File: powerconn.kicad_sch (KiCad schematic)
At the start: 13 parts, among them CN1 Conn_01x01, CN2 Conn_01x01, CN3 Conn_01x01, K1 HF32FV-16/5-HLTF(590), Q1 MMBT3904

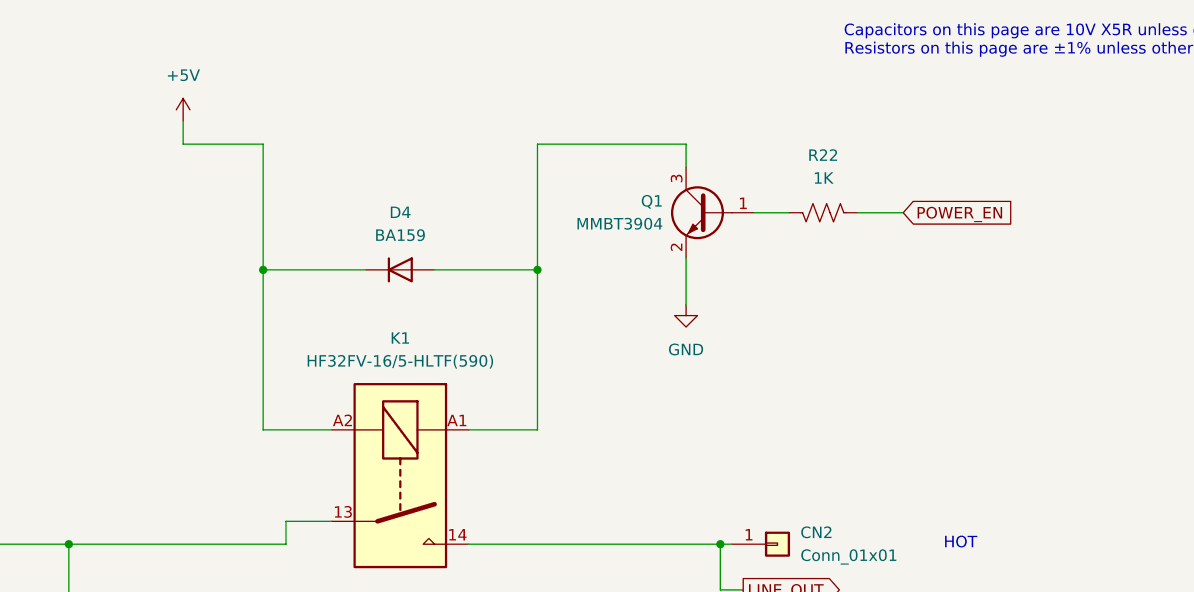
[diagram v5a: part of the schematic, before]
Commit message: All values determined for schematic. From measurements, datasheets, or reading markings.
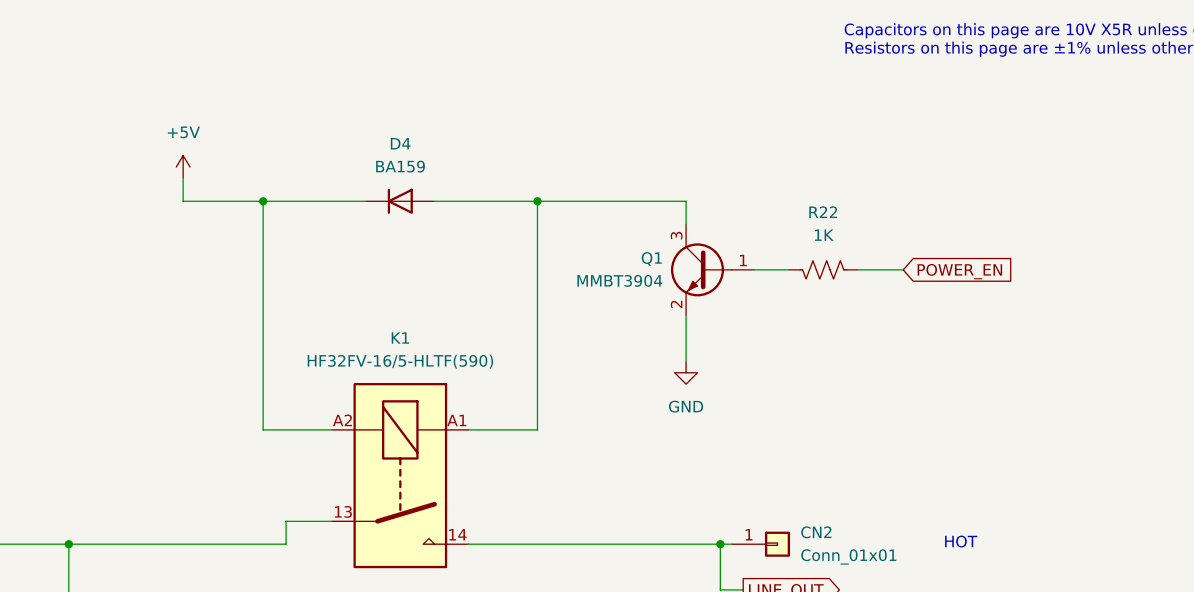
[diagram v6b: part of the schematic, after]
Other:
- moved on the sheet: D4, Q1, R22
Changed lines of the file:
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@@
 	)
 	(junction
-		(at 165.1 52.07)
+		(at 134.62 44.45)
 		(diameter 0)
 		(color 0 0 0 0)
@@
 	)
 	(junction
-		(at 134.62 52.07)
+		(at 165.1 44.45)
 		(diameter 0)
 		(color 0 0 0 0)
@@
 	(wire
 		(pts
-			(xy 153.67 52.07) (xy 165.1 52.07)
+			(xy 153.67 44.45) (xy 165.1 44.45)
 		)
 		(stroke
@@
 	(wire
 		(pts
-			(xy 181.61 38.1) (xy 181.61 40.64)
+			(xy 181.61 44.45) (xy 181.61 46.99)
 		)
 		(stroke
@@
 	(wire
 		(pts
-			(xy 205.74 45.72) (xy 200.66 45.72)
+			(xy 205.74 52.07) (xy 200.66 52.07)
 		)
 		(stroke
@@
 	(wire
 		(pts
-			(xy 181.61 38.1) (xy 165.1 38.1)
-		)
-		(stroke
-			(width 0)
-			(type default)
-		)
-	)
-	(wire
-		(pts
-			(xy 193.04 45.72) (xy 189.23 45.72)
+			(xy 181.61 44.45) (xy 165.1 44.45)
+		)
+		(stroke
+			(width 0)
+			(type default)
+		)
+	)
+	(wire
+		(pts
+			(xy 193.04 52.07) (xy 189.23 52.07)
 		)
 		(stroke
@@
 	(wire
 		(pts
-			(xy 134.62 38.1) (xy 134.62 52.07)
-		)
-		(stroke
-			(width 0)
-			(type default)
-		)
-	)
-	(wire
-		(pts
-			(xy 125.73 35.56) (xy 125.73 38.1)
+			(xy 125.73 41.91) (xy 125.73 44.45)
 		)
 		(stroke
@@
 	(wire
 		(pts
-			(xy 134.62 52.07) (xy 146.05 52.07)
+			(xy 134.62 44.45) (xy 146.05 44.45)
 		)
 		(stroke
@@
 	(wire
 		(pts
-			(xy 165.1 38.1) (xy 165.1 52.07)
-		)
-		(stroke
-			(width 0)
-			(type default)
-		)
-	)
-	(wire
-		(pts
 			(xy 157.48 82.55) (xy 185.42 82.55)
 		)
@@
 	(wire
 		(pts
-			(xy 134.62 52.07) (xy 134.62 69.85)
-		)
-		(stroke
-			(width 0)
-			(type default)
-		)
-	)
-	(wire
-		(pts
-			(xy 165.1 52.07) (xy 165.1 69.85)
-		)
-		(stroke
-			(width 0)
-			(type default)
-		)
-	)
-	(wire
-		(pts
-			(xy 181.61 50.8) (xy 181.61 55.88)
+			(xy 165.1 44.45) (xy 165.1 69.85)
+		)
+		(stroke
+			(width 0)
+			(type default)
+		)
+	)
+	(wire
+		(pts
+			(xy 181.61 57.15) (xy 181.61 62.23)
 		)
 		(stroke
@@
 	(wire
 		(pts
-			(xy 125.73 38.1) (xy 134.62 38.1)
+			(xy 125.73 44.45) (xy 134.62 44.45)
 		)
 		(stroke
@@
 		(pts
 			(xy 137.16 80.01) (xy 142.24 80.01)
+		)
+		(stroke
+			(width 0)
+			(type default)
+		)
+	)
+	(wire
+		(pts
+			(xy 134.62 44.45) (xy 134.62 69.85)
 		)
 		(stroke
@@
 	(global_label "POWER_EN"
 		(shape input)
-		(at 205.74 45.72 0)
+		(at 205.74 52.07 0)
 		(fields_autoplaced yes)
 		(effects
@@
 		)
 		(property "Intersheetrefs" "${INTERSHEET_REFS}"
-			(at 218.6432 45.72 0)
+			(at 218.6432 52.07 0)
 			(effects
 				(font
@@
 	(symbol
 		(lib_id "Diode:BA159")
-		(at 149.86 52.07 0)
+		(at 149.86 44.45 0)
 		(unit 1)
 		(exclude_from_sim no)
@@
 		(fields_autoplaced yes)
 		(property "Reference" "D4"
-			(at 149.86 45.72 0)
+			(at 149.86 38.1 0)
 			(effects
 				(font
@@
 		)
 		(property "Value" "BA159"
-			(at 149.86 48.26 0)
+			(at 149.86 40.64 0)
 			(effects
 				(font
@@
 		)
 		(property "Footprint" "Diode_SMD:D_SOD-123F"
-			(at 149.86 56.515 0)
+			(at 149.86 48.895 0)
 			(effects
 				(font
@@
 		)
 		(property "Datasheet" "https://www.vishay.com/docs/88536/ba157.pdf"
-			(at 149.86 52.07 0)
+			(at 149.86 44.45 0)
 			(effects
 				(font
@@
 		)
 		(property "Description" "1000V 1A Fast recovery Rectifier Diode, DO-41"
-			(at 149.86 52.07 0)
+			(at 149.86 44.45 0)
 			(effects
 				(font
@@
 		)
 		(property "Sim.Device" "D"
-			(at 149.86 52.07 0)
+			(at 149.86 44.45 0)
 			(effects
 				(font
@@
 		)
 		(property "Sim.Pins" "1=K 2=A"
-			(at 149.86 52.07 0)
+			(at 149.86 44.45 0)
 			(effects
 				(font
@@
 	(symbol
 		(lib_id "Device:R_US")
-		(at 196.85 45.72 270)
+		(at 196.85 52.07 270)
 		(mirror x)
 		(unit 1)
@@
 		(fields_autoplaced yes)
 		(property "Reference" "R22"
-			(at 196.85 39.37 90)
+			(at 196.85 45.72 90)
 			(effects
 				(font
@@
 		)
 		(property "Value" "1K"
-			(at 196.85 41.91 90)
+			(at 196.85 48.26 90)
 			(effects
 				(font
@@
 		)
 		(property "Footprint" "Resistor_SMD:R_0402_1005Metric"
-			(at 196.596 44.704 90)
+			(at 196.596 51.054 90)
 			(effects
 				(font
@@
 		)
 		(property "Datasheet" "~"
-			(at 196.85 45.72 0)
+			(at 196.85 52.07 0)
 			(effects
 				(font
@@
 		)
 		(property "Description" "Resistor, US symbol"
-			(at 196.85 45.72 0)
+			(at 196.85 52.07 0)
 			(effects
 				(font
@@
 	(symbol
 		(lib_id "power:GND")
-		(at 181.61 55.88 0)
+		(at 181.61 62.23 0)
 		(mirror y)
 		(unit 1)
@@
 		(fields_autoplaced yes)
 		(property "Reference" "#PWR013"
+			(at 181.61 68.58 0)
+			(effects
+				(font
+					(size 1.27 1.27)
+				)
+				(hide yes)
+			)
+		)
+		(property "Value" "GND"
+			(at 181.61 67.31 0)
+			(effects
+				(font
+					(size 1.27 1.27)
+				)
+			)
+		)
+		(property "Footprint" ""
 			(at 181.61 62.23 0)
 			(effects
@@
 			)
 		)
-		(property "Value" "GND"
-			(at 181.61 60.96 0)
-			(effects
-				(font
-					(size 1.27 1.27)
-				)
-			)
-		)
-		(property "Footprint" ""
-			(at 181.61 55.88 0)
-			(effects
-				(font
-					(size 1.27 1.27)
-				)
-				(hide yes)
-			)
-		)
 		(property "Datasheet" ""
-			(at 181.61 55.88 0)
+			(at 181.61 62.23 0)
 			(effects
 				(font
@@
 		)
 		(property "Description" "Power symbol creates a global label with name \"GND\" , ground"
-			(at 181.61 55.88 0)
+			(at 181.61 62.23 0)
 			(effects
 				(font
@@
 	(symbol
 		(lib_id "power:+5V")
-		(at 125.73 35.56 0)
+		(at 125.73 41.91 0)
 		(mirror y)
 		(unit 1)
@@
 		(fields_autoplaced yes)
 		(property "Reference" "#PWR021"
-			(at 125.73 39.37 0)
+			(at 125.73 45.72 0)
 			(effects
 				(font
@@
 		)
 		(property "Value" "+5V"
-			(at 125.73 30.48 0)
+			(at 125.73 36.83 0)
 			(effects
 				(font
@@
 		)
 		(property "Footprint" ""
-			(at 125.73 35.56 0)
+			(at 125.73 41.91 0)
 			(effects
 				(font
@@
 		)
 		(property "Datasheet" ""
-			(at 125.73 35.56 0)
+			(at 125.73 41.91 0)
 			(effects
 				(font
@@
 		)
 		(property "Description" "Power symbol creates a global label with name \"+5V\""
-			(at 125.73 35.56 0)
+			(at 125.73 41.91 0)
 			(effects
 				(font
@@
 	(symbol
 		(lib_id "Transistor_BJT:MMBT3904")
-		(at 184.15 45.72 0)
+		(at 184.15 52.07 0)
 		(mirror y)
 		(unit 1)
@@
 		(fields_autoplaced yes)
 		(property "Reference" "Q1"
-			(at 179.07 44.4499 0)
+			(at 179.07 50.7999 0)
 			(effects
 				(font
@@
 		)
 		(property "Value" "MMBT3904"
-			(at 179.07 46.9899 0)
+			(at 179.07 53.3399 0)
 			(effects
 				(font
@@
 		)
 		(property "Footprint" "Package_TO_SOT_SMD:SOT-23"
-			(at 179.07 47.625 0)
+			(at 179.07 53.975 0)
 			(effects
 				(font
@@
 		)
 		(property "Datasheet" "https://www.onsemi.com/pdf/datasheet/pzt3904-d.pdf"
-			(at 184.15 45.72 0)
+			(at 184.15 52.07 0)
 			(effects
 				(font
@@
 		)
 		(property "Description" "0.2A Ic, 40V Vce, Small Signal NPN Transistor, SOT-23"
-			(at 184.15 45.72 0)
-			(effects
-				(font
+			(at 184.15 52.07 0)
+			(effects
+				(font

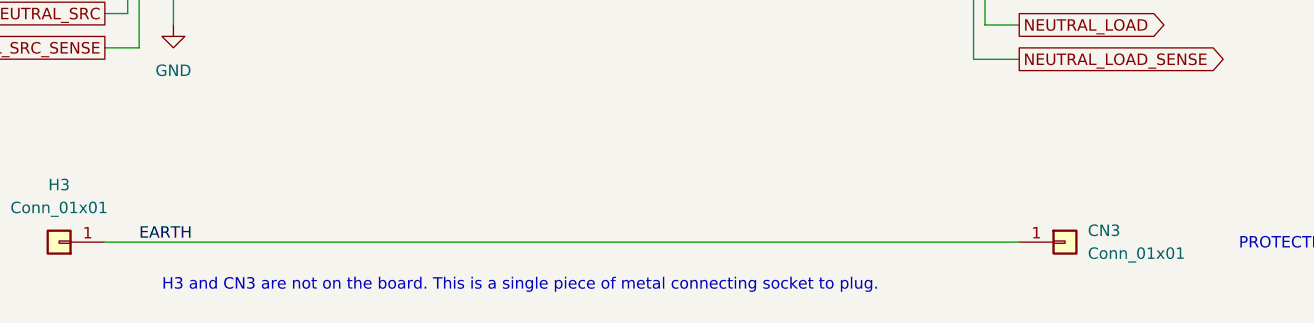
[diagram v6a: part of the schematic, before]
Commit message: Fixed plug and receptacle foots. No components left to fix but L1? And the silk and fab layers. And some kind of labeling of the design.
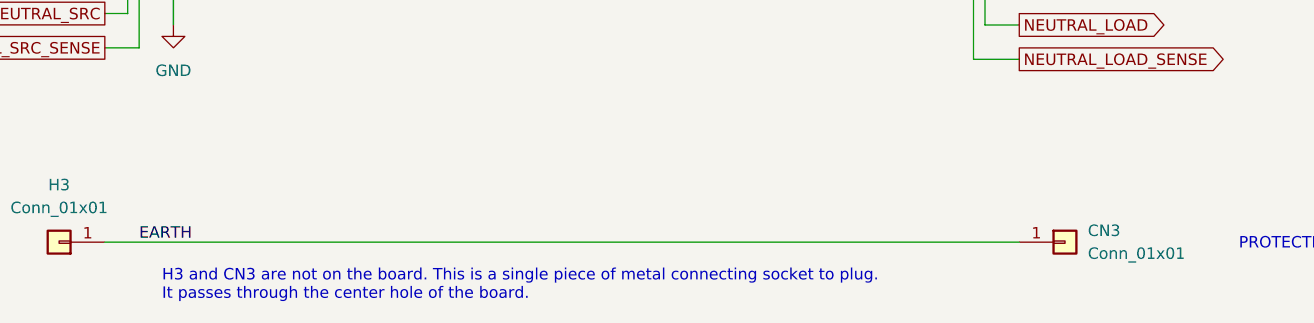
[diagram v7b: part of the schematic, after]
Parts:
- CN1, CN2: footprint Connector_PinHeader_2.54mm:PinHeader_1x01_P2.54mm_Vertical -> HF relays:NEMA5R_blade; now left out of the parts list
- H1, H2: footprint Connector_PinHeader_2.54mm:PinHeader_1x01_P2.54mm_Vertical -> HF relays:NEMA5P_post; now left out of the parts list
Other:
- note added: "H3 and CN3 are not on the board. This is a single piece of metal connecting socket to plug. It passes through the center hole of the board."
- note removed: "H3 and CN3 are not on the board. This is a single piece of metal connecting socket to plug."
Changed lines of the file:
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@@
 		)
 	)
-	(text "H3 and CN3 are not on the board. This is a single piece of metal connecting socket to plug."
+	(text "H3 and CN3 are not on the board. This is a single piece of metal connecting socket to plug.\nIt passes through the center hole of the board."
 		(exclude_from_sim no)
 		(at 91.44 162.306 0)
@@
 		(unit 1)
 		(exclude_from_sim no)
-		(in_bom yes)
+		(in_bom no)
 		(on_board yes)
 		(dnp no)
@@
 			)
 		)
-		(property "Footprint" "Connector_PinHeader_2.54mm:PinHeader_1x01_P2.54mm_Vertical"
+		(property "Footprint" "HF relays:NEMA5P_post"
 			(at 80.01 127 0)
 			(effects
@@
 		(unit 1)
 		(exclude_from_sim no)
-		(in_bom yes)
+		(in_bom no)
 		(on_board yes)
 		(dnp no)
@@
 			)
 		)
-		(property "Footprint" "Connector_PinHeader_2.54mm:PinHeader_1x01_P2.54mm_Vertical"
+		(property "Footprint" "HF relays:NEMA5P_post"
 			(at 80.01 82.55 0)
 			(effects
@@
 		(unit 1)
 		(exclude_from_sim no)
-		(in_bom yes)
+		(in_bom no)
 		(on_board yes)
 		(dnp no)
@@
 			)
 		)
-		(property "Footprint" "Connector_PinHeader_2.54mm:PinHeader_1x01_P2.54mm_Vertical"
+		(property "Footprint" "HF relays:NEMA5R_blade"
 			(at 191.77 127 0)
 			(effects
@@
 		(unit 1)
 		(exclude_from_sim no)
-		(in_bom yes)
+		(in_bom no)
 		(on_board yes)
 		(dnp no)
@@
 			)
 		)
-		(property "Footprint" "Connector_PinHeader_2.54mm:PinHeader_1x01_P2.54mm_Vertical"
+		(property "Footprint" "HF relays:NEMA5R_blade"
 			(at 191.77 82.55 0)
 			(effects

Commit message: Fixed silk, fixed fab. Fixed a few part 3D models. Starting to rename stuff.
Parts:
- CN1, CN2, H1, H2: now in the parts list
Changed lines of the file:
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@@
 	(title_block
 		(title "power connections and control")
-		(date "2025-07-25")
+		(date "2025-07-28")
 	)
 	(text "Capacitors on this page are 10V X5R unless otherwise noted.\nResistors on this page are ±1% unless otherwise noted."
@@
 		(unit 1)
 		(exclude_from_sim no)
-		(in_bom no)
+		(in_bom yes)
 		(on_board yes)
 		(dnp no)
@@
 		(unit 1)
 		(exclude_from_sim no)
-		(in_bom no)
+		(in_bom yes)
 		(on_board yes)
 		(dnp no)
@@
 		(unit 1)
 		(exclude_from_sim no)
-		(in_bom no)
+		(in_bom yes)
 		(on_board yes)
 		(dnp no)
@@
 		(unit 1)
 		(exclude_from_sim no)
-		(in_bom no)
+		(in_bom yes)
 		(on_board yes)
 		(dnp no)
